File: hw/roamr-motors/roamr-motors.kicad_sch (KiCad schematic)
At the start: 22 parts, among them J1 JST_XH_S2B-XH-A-1, J10 JST_SH_BM06B-SRSS-TB, J2 USB4215-03-A, J3 USB4215-03-A, J4 JST_XH_S2B-XH-A-1, J5 JST_XH_S2B-XH-A-1, J6 JST_PH_B3B-PH-SM4-TB, J7 JST_SH_BM06B-SRSS-TB, J8 JST_XH_S2B-XH-A-1, J9 JST_PH_B3B-PH-SM4-TB

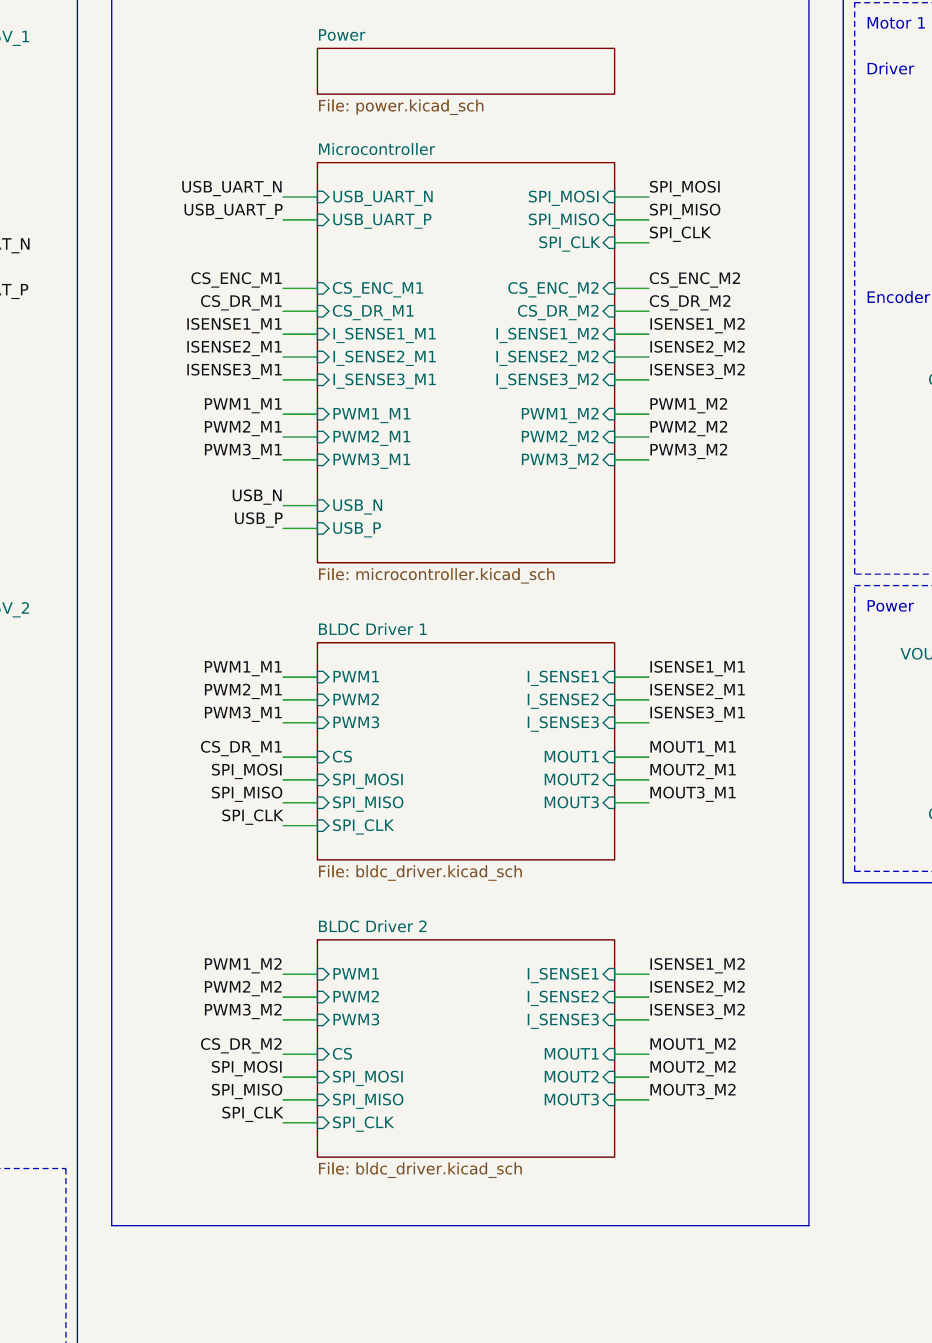
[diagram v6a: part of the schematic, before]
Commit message: layout done except i need to add two fuses
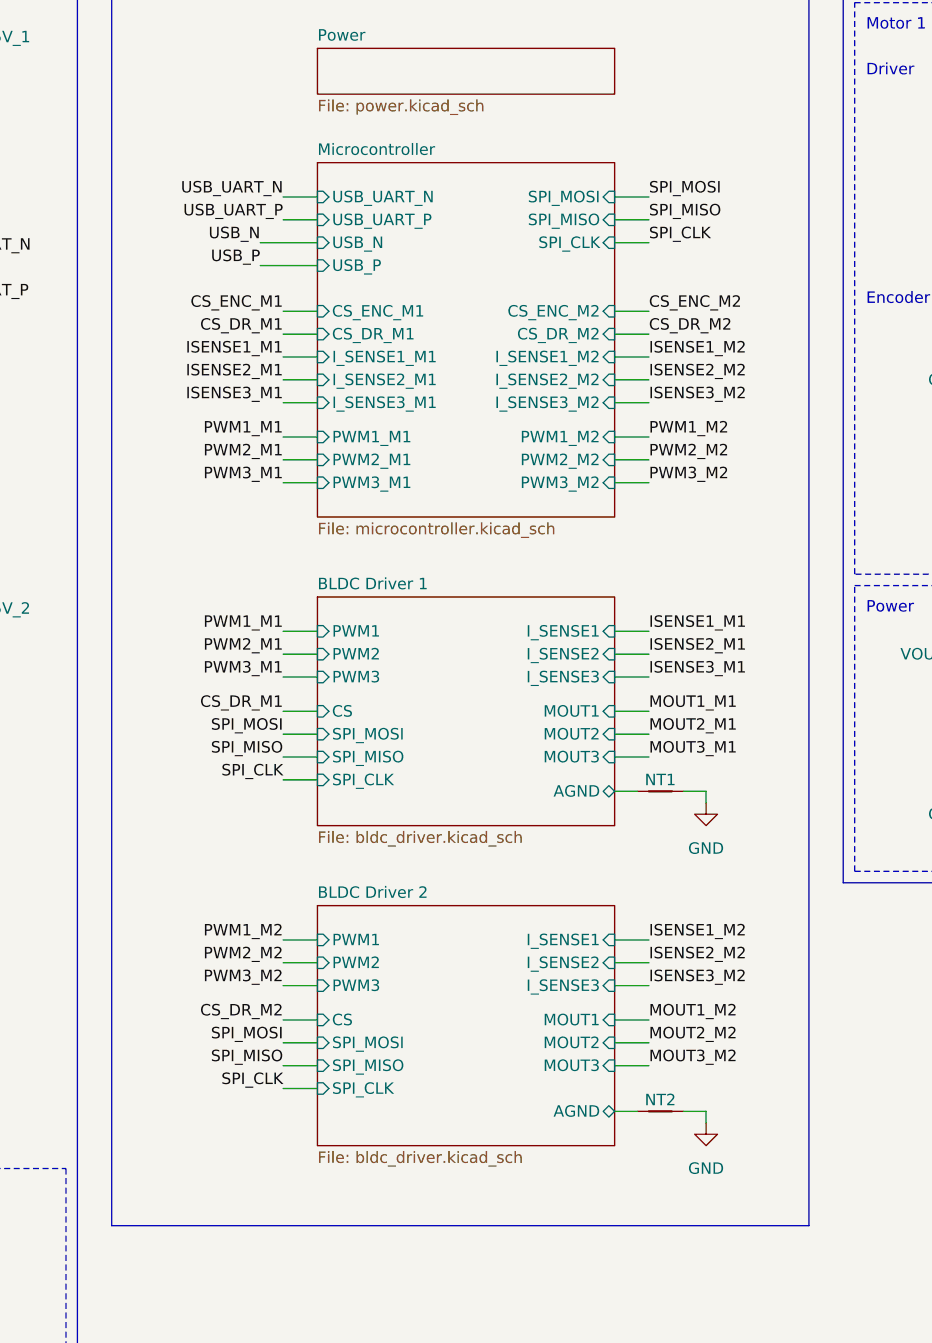
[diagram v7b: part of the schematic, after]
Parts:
- added NT1, NT2: NetTie_2, NetTie:NetTie-2_SMD_Pad0.5mm, symbol Device:NetTie_2
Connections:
- net GND: now also NT1.2, NT2.2
- new net BLDC Driver 1/AGND: NT1.1
- new net BLDC Driver 2/AGND: NT2.1
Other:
- sheet BLDC Driver 1 ports: added AGND; removed none
- sheet BLDC Driver 2 ports: added AGND; removed none

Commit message: i don't remember what this change was but probably fuses?
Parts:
- added F1, F2: 0466005.NRHF, 0466005:F1206, symbol 0466005:0466005.NRHF
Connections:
- net VIN_12V: now also F1.1; no longer J1.1 (Pin_1)
- net VIN_5V: now also F2.1; no longer J4.1 (Pin_1)
- new net: F1.2, J1.1 (Pin_1)
- new net: F2.2, J4.1 (Pin_1)
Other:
- moved on the sheet: D1, D2, D3, D4, D5, D6, D7, D8, J1, J10, J2, J3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
